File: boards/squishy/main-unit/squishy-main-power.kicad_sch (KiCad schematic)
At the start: 159 parts, among them J5 Jack-DC, Q1 NTMFS5C442NT1G, Q10 PFET, Q2 NX6008NBKR, Q3 NX6008NBKR, Q4 NX6008NBKR, Q5 NX6008NBKR, Q6 PMPB20EN, Q8 DMN65D8L-7, SW1 RST, U1 LFE5UM5G-45F-8BG381C, U13 LM51551DSSR, U18 HyperRAM, U19 HyperRAM, U2 GD25Q64EWIGR, U21 AP3428/A, U5 APX811-40UG-7, U7 TPS73733DRVR, U8 TPS7A1125PDRVT, U9 TPS7A1112PDRVT

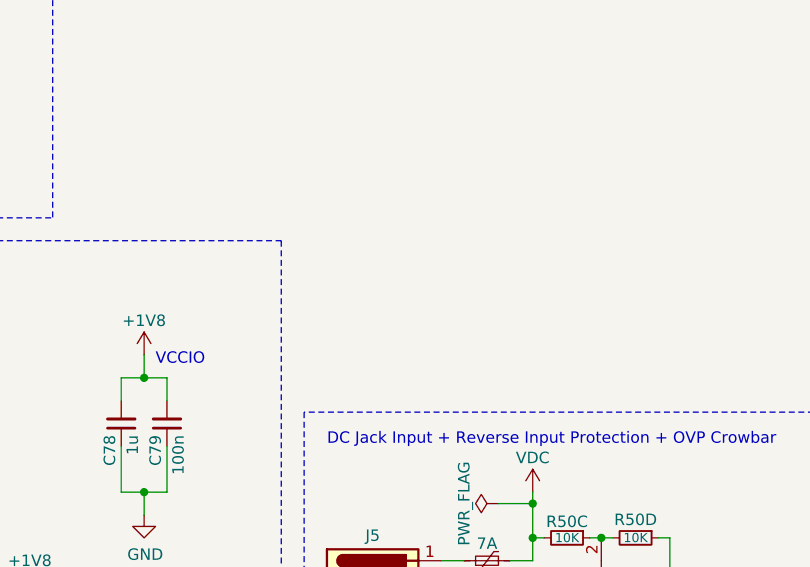
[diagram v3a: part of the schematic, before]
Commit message: squishy: main: Cleaned up the SCSI PHY current sense stuff and de-brain-sluged the PHY connector
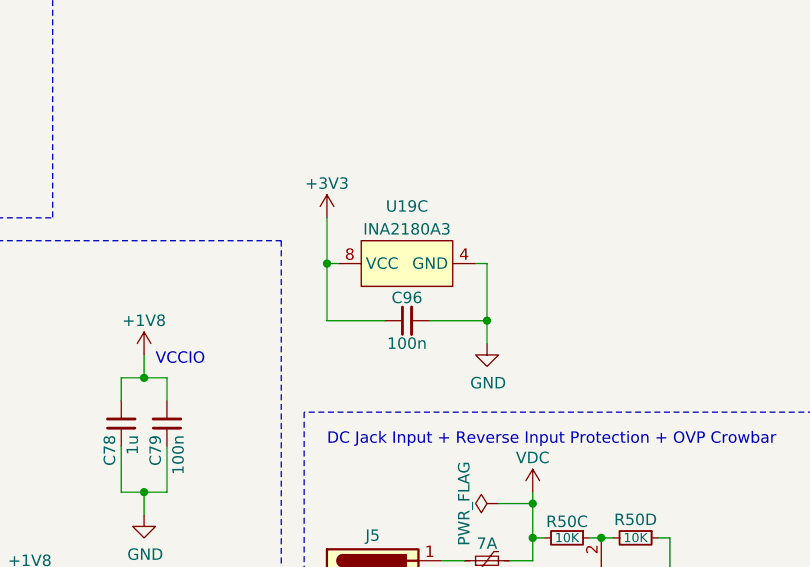
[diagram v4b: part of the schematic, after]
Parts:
- added C96: 100n, Capacitor_SMD:C_0603_1608Metric, symbol Device:C_Small
- added unit 3 of U19
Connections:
- net +3V3: now also C96.1, U19.8 (VCC)
- net GND: now also C96.2, U19.4 (GND), U19.9 (GND)
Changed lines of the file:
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@@
   (junction (at 69.85 259.08) (diameter 0) (color 0 0 0 0)
   )
+  (junction (at 173.99 96.52) (diameter 0) (color 0 0 0 0)
+  )
   (junction (at 207.01 208.28) (diameter 0) (color 0 0 0 0)
   )
@@
   (junction (at 57.15 138.43) (diameter 0) (color 0 0 0 0)
   )
+  (junction (at 156.21 90.17) (diameter 0) (color 0 0 0 0)
+  )
   (junction (at 116.84 137.16) (diameter 0) (color 0 0 0 0)
   )
@@
     (stroke (width 0) (type default))
   )
+  (wire (pts (xy 156.21 85.09) (xy 156.21 90.17))
+    (stroke (width 0) (type default))
+  )
   (polyline (pts (xy 201.93 146.05) (xy 201.93 182.88))
     (stroke (width 0) (type dash))
@@
     (stroke (width 0) (type default))
   )
+  (wire (pts (xy 167.64 96.52) (xy 173.99 96.52))
+    (stroke (width 0) (type default))
+  )
   (polyline (pts (xy 377.19 146.05) (xy 377.19 132.08))
     (stroke (width 0) (type dash))
@@
     (stroke (width 0) (type default))
   )
+  (wire (pts (xy 156.21 90.17) (xy 156.21 96.52))
+    (stroke (width 0) (type default))
+  )
   (wire (pts (xy 233.68 163.83) (xy 233.68 166.37))
     (stroke (width 0) (type default))
@@
     (stroke (width 0) (type default))
   )
+  (wire (pts (xy 156.21 90.17) (xy 157.48 90.17))
+    (stroke (width 0) (type default))
+  )
   (wire (pts (xy 76.2 36.83) (xy 76.2 39.37))
     (stroke (width 0) (type default))
@@
     (stroke (width 0) (type default))
   )
+  (wire (pts (xy 173.99 96.52) (xy 173.99 99.06))
+    (stroke (width 0) (type default))
+  )
   (wire (pts (xy 281.94 182.88) (xy 289.56 182.88))
     (stroke (width 0) (type default))
@@
     (stroke (width 0) (type default))
   )
+  (wire (pts (xy 173.99 90.17) (xy 173.99 96.52))
+    (stroke (width 0) (type default))
+  )
   (wire (pts (xy 391.16 137.16) (xy 393.7 137.16))
     (stroke (width 0) (type default))
@@
     (stroke (width 0) (type default))
   )
+  (wire (pts (xy 156.21 96.52) (xy 162.56 96.52))
+    (stroke (width 0) (type default))
+  )
   (wire (pts (xy 208.28 267.97) (xy 208.28 271.78))
     (stroke (width 0) (type default))
@@
     (stroke (width 0) (type default))
   )
+  (wire (pts (xy 172.72 90.17) (xy 173.99 90.17))
+    (stroke (width 0) (type default))
+  )
   (wire (pts (xy 55.88 186.69) (xy 63.5 186.69))
     (stroke (width 0) (type default))
@@
     )
   )
+  (symbol (lib_id "power:GND") (at 173.99 99.06 0) (unit 1)
+    (in_bom yes) (on_board yes) (dnp no)
+    (property "Reference" "#PWR0147" (at 173.99 105.41 0)
+      (effects (font (size 1.27 1.27)) hide)
+    )
+    (property "Value" "GND" (at 174.117 103.4542 0)
+      (effects (font (size 1.27 1.27)))
+    )
+    (property "Footprint" "" (at 173.99 99.06 0)
+      (effects (font (size 1.27 1.27)) hide)
+    )
+    (property "Datasheet" "" (at 173.99 99.06 0)
+      (effects (font (size 1.27 1.27)) hide)
+    )
+    (pin "1")
+    (instances
+      (project "squishy-main"
+        (path "/d4567381-92dd-4d3b-8c64-40007ced30aa/3a0401a0-2db0-4f5c-bc8b-66f50b74dd32"
+          (reference "#PWR0147") (unit 1)
+        )
+      )
+    )
+  )
   (symbol (lib_id "DX-MON:pkl_R4_Small") (at 20.32 43.18 180) (unit 4)
     (in_bom yes) (on_board yes) (dnp no)
@@
     )
   )
+  (symbol (lib_id "Device:C_Small") (at 165.1 96.52 90) (unit 1)
+    (in_bom yes) (on_board yes) (dnp no)
+    (property "Reference" "C96" (at 165.1 93.98 90)
+      (effects (font (size 1.27 1.27)))
+    )
+    (property "Value" "100n" (at 165.1 99.06 90)
+      (effects (font (size 1.27 1.27)))
+    )
+    (property "Footprint" "Capacitor_SMD:C_0603_1608Metric" (at 165.1 96.52 0)
+      (effects (font (size 1.27 1.27)) hide)
+    )
+    (property "Datasheet" "https://content.kemet.com/datasheets/KEM_C1006_X5R_SMD.pdf" (at 165.1 96.52 0)
+      (effects (font (size 1.27 1.27)) hide)
+    )
+    (property "MFR" "KEMET" (at 165.1 96.52 90)
+      (effects (font (size 1.27 1.27)) hide)
+    )
+    (property "MPN" "C0402C104M8PACTU" (at 165.1 96.52 90)
+      (effects (font (size 1.27 1.27)) hide)
+    )
+    (pin "1")
+    (pin "2")
+    (instances
+      (project "squishy-main"
+        (path "/d4567381-92dd-4d3b-8c64-40007ced30aa/3a0401a0-2db0-4f5c-bc8b-66f50b74dd32"
+          (reference "C96") (unit 1)
+        )
+      )
+    )
+  )
   (symbol (lib_id "Mechanical:MountingHole_Pad") (at 391.16 132.08 0) (unit 1)
     (in_bom no) (on_board yes) (dnp no)
@@
     )
   )
+  (symbol (lib_name "INAx180_1") (lib_id "lethalbit-analog:INAx180") (at 165.1 90.17 0) (unit 3)
+    (in_bom yes) (on_board yes) (dnp no)
+    (property "Reference" "U19" (at 165.1 83.82 0)
+      (effects (font (size 1.27 1.27)))
+    )
+    (property "Value" "INA2180A3" (at 165.1 86.36 0)
+      (effects (font (size 1.27 1.27)))
+    )
+    (property "Footprint" "lethalbit:WSON_8_2x2mm_1EP" (at 165.1 81.28 0)
+      (effects (font (size 1.27 1.27)) hide)
+    )
+    (property "Datasheet" "https://www.ti.com/lit/ds/symlink/ina2180.pdf" (at 165.1 81.28 0)
+      (effects (font (size 1.27 1.27)) hide)
+    )
+    (property "MFR" "Texas Instruments" (at 165.1 81.28 0)
+      (effects (font (size 1.27 1.27)) hide)
+    )
+    (property "MPN" "INA2180A3IDSGR" (at 165.1 81.28 0)
+      (effects (font (size 1.27 1.27)) hide)
+    )
+    (pin "1")
+    (pin "2")
+    (pin "3")
+    (pin "5")
+    (pin "6")
+    (pin "7")
+    (pin "4")
+    (pin "8")
+    (pin "9")
+    (instances
+      (project "squishy-main"
+        (path "/d4567381-92dd-4d3b-8c64-40007ced30aa/3a0401a0-2db0-4f5c-bc8b-66f50b74dd32"
+          (reference "U19") (unit 3)
+        )
+      )
+    )
+  )
   (symbol (lib_id "power:GND") (at 223.52 175.26 0) (unit 1)
     (in_bom yes) (on_board yes) (dnp no)
@@
         )
       )
+    )
+  )
+  (symbol (lib_id "power:+3V3") (at 156.21 85.09 0) (unit 1)
+    (in_bom yes) (on_board yes) (dnp no)
+    (property "Reference" "#PWR0148" (at 156.21 88.9 0)
+      (effects (font (size 1.27 1.27)) hide)
+    )
+    (property "Value" "+3V3" (at 156.21 81.28 0)
+      (effects (font (size 1.27 1.27)))
+    )
+    (property "Footprint" "" (at 156.21 85.09 0)
+      (effects (font (size 1.27 1.27)) hide)
+    )
+    (property "Datasheet" "" (at 156.21 85.09 0)
+      (effects (font (size 1.27 1.27)) hide)
+    )
+    (pin "1")
+    (instances
+      (project "squishy-main"
+        (path "/d4567381-92dd-4d3b-8c64-40007ced30aa/3a0401a0-2db0-4f5c-bc8b-66f50b74dd32"
+          (reference "#PWR0148") (unit 1)
+        )
+      )

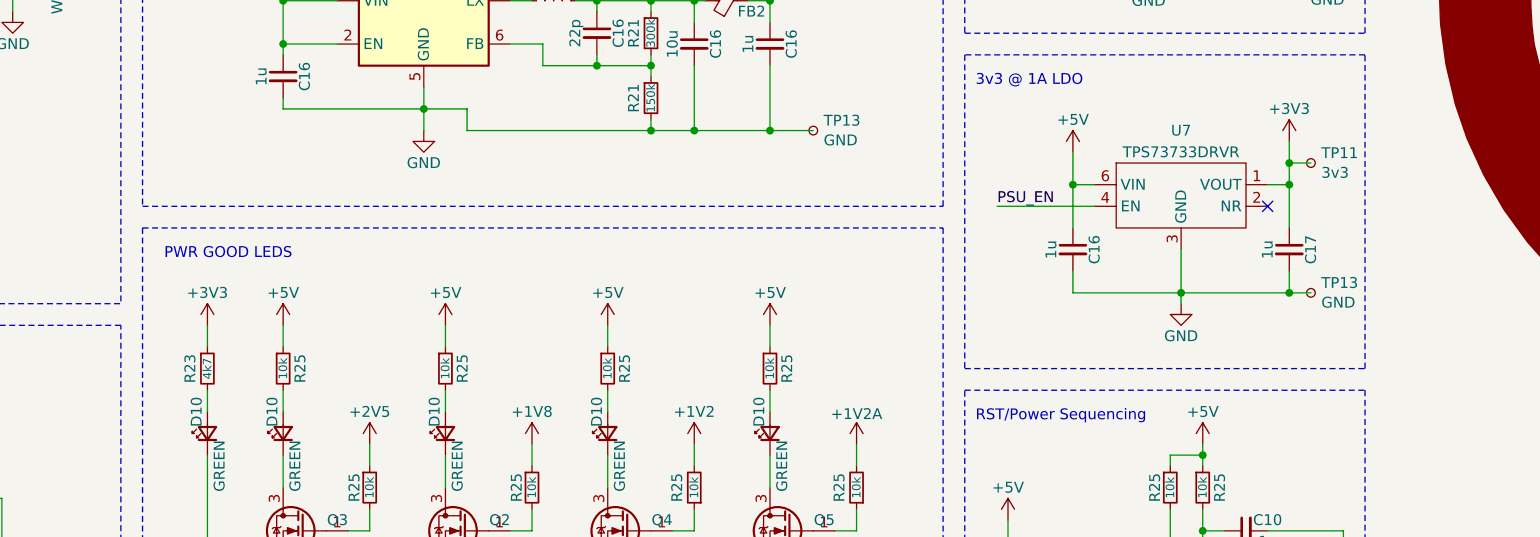
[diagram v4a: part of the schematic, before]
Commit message: squishy: main: Added notes about if we really want the 1v8 buck hanging off the 3v3 LDO, and that we might need to up the 3v3 LDO from 1A to larger
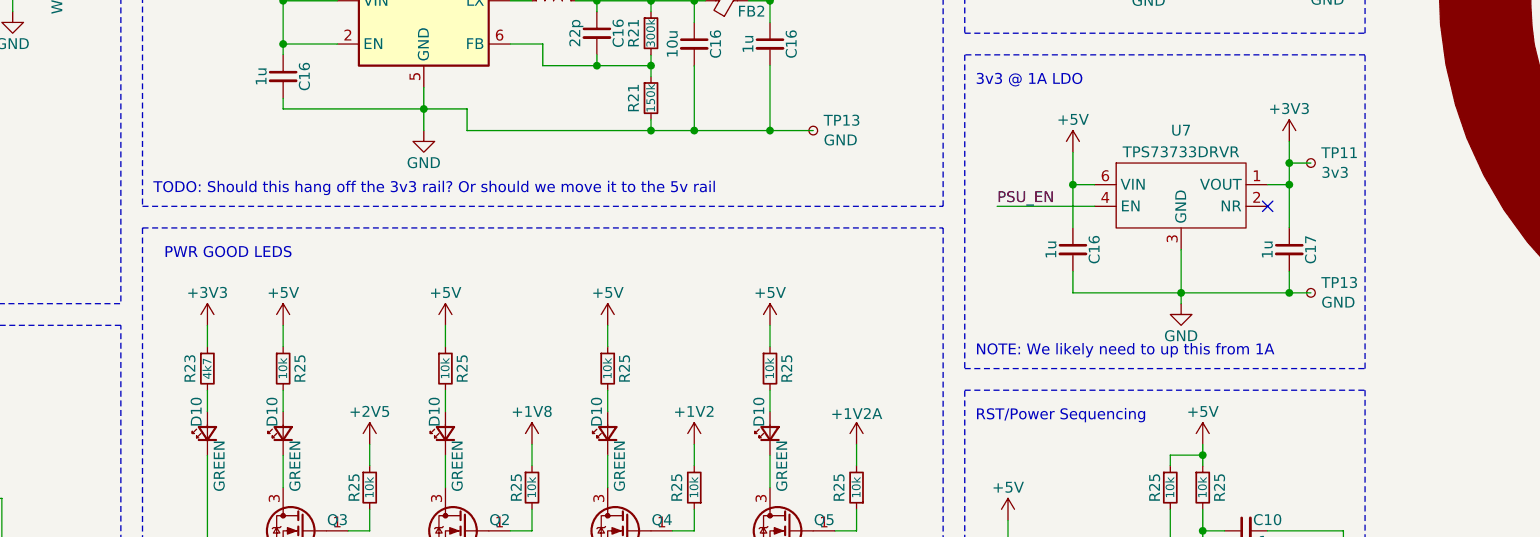
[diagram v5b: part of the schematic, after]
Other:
- note added: "NOTE: We likely need to up this from 1A"
- note added: "TODO: Should this hang off the 3v3 rail? Or should we move it to the 5v rail"
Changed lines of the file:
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@@
+    (effects (font (size 1.27 1.27)) (justify left bottom))
+  )
+  (text "NOTE: We likely need to up this from 1A\n" (at 251.46 242.57 0)
     (effects (font (size 1.27 1.27)) (justify left bottom))
   )
@@
     (effects (font (size 1.27 1.27)) (justify left bottom))
   )
+  (text "TODO: Should this hang off the 3v3 rail? Or should we move it to the 5v rail"
+    (at 154.94 223.52 0)
+    (effects (font (size 1.27 1.27)) (justify left bottom))
+  )

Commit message: squishy: main: Some final cleanup, made ERC clean, hooked up some more rough ordering for IO pins for the SCSI PHY, Replaced the 3v3 LDO with a buck due to other rails hanging off of it.
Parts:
- removed C16, C17: 1u, Capacitor_SMD:C_0603_1608Metric, symbol Device:C_Small
- removed TP13: GND, TestPoint:TestPoint_Pad_D1.0mm, symbol Connector:TestPoint_Small
- removed U7: TPS73733DRVR, Package_SON:WSON-6-1EP_2x2mm_P0.65mm_EP1x1.6mm, symbol lethalbit-power:TPS737xx
- added C101: 22u, Capacitor_SMD:C_0603_1608Metric, symbol Device:C_Small
- added C46: 10u, Capacitor_SMD:C_0603_1608Metric, symbol Device:C_Small
- added L3: 1u, lethalbit-inductor:L_Vishay_IHLP-3232, symbol Device:L
- added R55: 249k, Resistor_SMD:R_0603_1608Metric, symbol Device:R_Small
- added R56: 39k2, Resistor_SMD:R_0603_1608Metric, symbol Device:R_Small
- added R57: 178k, Resistor_SMD:R_0603_1608Metric, symbol Device:R_Small
- added TP47: SEPIC_GOOD, TestPoint:TestPoint_Pad_D1.0mm, symbol Connector:TestPoint_Small
- added TP7: GND, TestPoint:TestPoint_Pad_D1.0mm, symbol Connector:TestPoint_Small
- added U23: TLV62084ADSGx, Package_SON:WSON-8-1EP_2x2mm_P0.5mm_EP0.9x1.6mm, symbol Regulator_Switching:TLV62084ADSGx
- U19: value INA2180A3 -> INA2180A1; MPN INA2180A3IDSGR -> INA2180A1IDSGR
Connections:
- net +1V2: no longer C33.1, R25.2, TP12.1, U1.T15 (VCCA1), U1.T6 (VCCA0), U1.U15 (VCCA1), U1.U6 (VCCA0), U8.3 (EN), U9.1 (VOUT), U9.2 (NC)
- net +3V3: now also U1.F10 (VCCIO0), U1.F11 (VCCIO1), U1.F12 (VCCIO1), U1.F9 (VCCIO0), U1.H6 (VCCIO7), U1.H7 (VCCIO7), U1.J6 (VCCIO7), C101.1, L3.2, R55.2, R57.1, U23.5 (VOS); no longer C16.1, U21.3 (VIN)
- net +5V: now also C16.1, U21.3 (VIN), C46.1, U23.8 (VIN)
- net GND: now also C101.2, C46.2, R56.2, TP7.1, U23.2 (GND), U23.3 (GND), U23.9 (GND)
- net PSU_EN: now also U23.1 (EN)
- net SEPIC_GOOD: now also TP47.1
- new net: L3.1, U23.7 (SW)
- new net: R57.2, U23.6 (PG)
- new net: R55.1, R56.1, U23.4 (FB)
- new net +1V2A: C33.1, R25.2, TP12.1, U1.T15 (VCCA1), U1.T6 (VCCA0), U1.U15 (VCCA1), U1.U6 (VCCA0), U8.3 (EN), U9.1 (VOUT), U9.2 (NC)
- no-connect marks 3 -> 2
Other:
- note added: "3v3 Buck"
- note added: "CSA"
- note removed: "3v3 @ 1A LDO"
- note removed: "NOTE: We likely need to up this from 1A"
- note removed: "TODO: Should this hang off the 3v3 rail? Or should we move it to the 5v rail"
- moved on the sheet: C16, C27, C32, C33, C96, FB2, L2, R21, TP11, TP12, TP13, TP17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

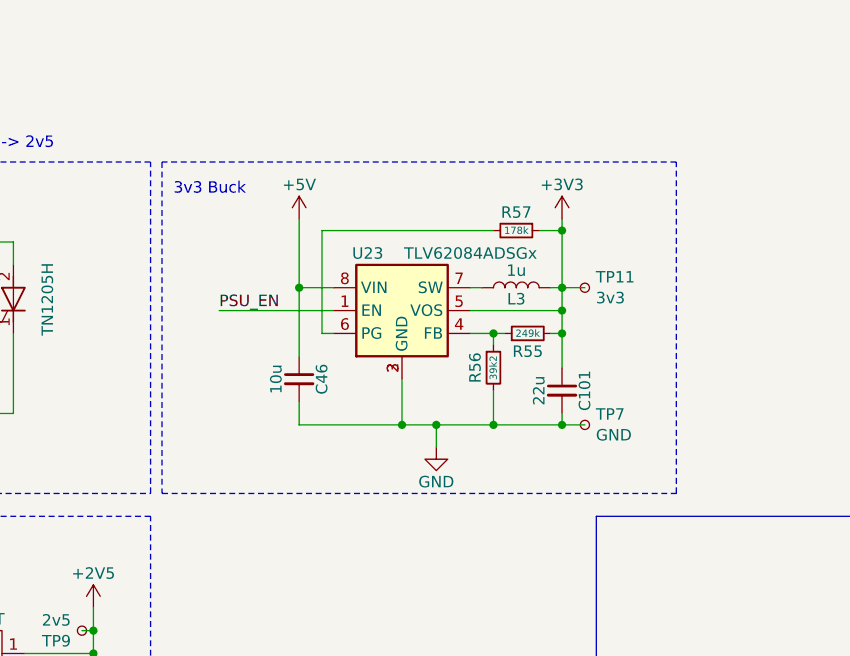
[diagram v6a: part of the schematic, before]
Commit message: squishy: main: Added the missing footprint for Q7
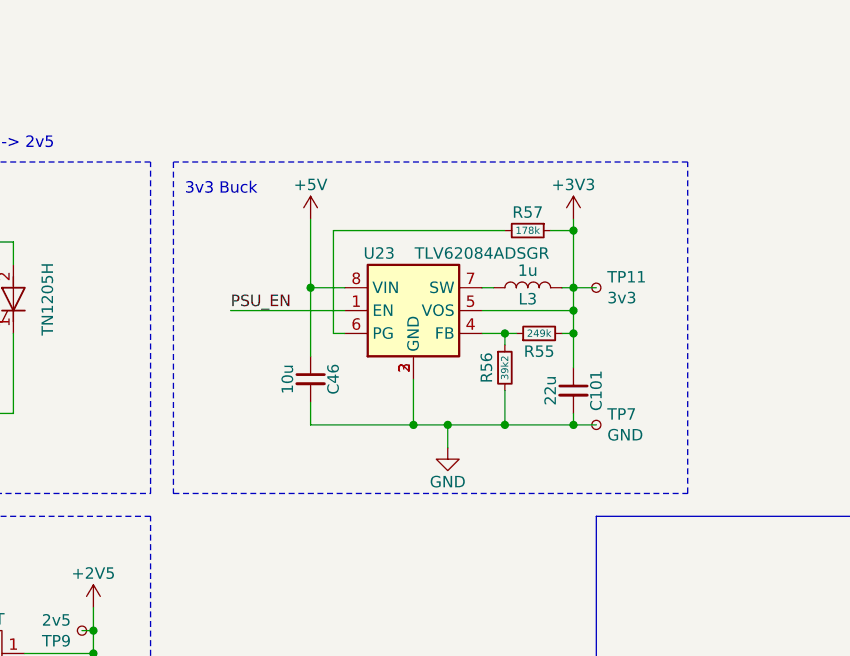
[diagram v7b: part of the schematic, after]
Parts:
- U23: value TLV62084ADSGx -> TLV62084ADSGR
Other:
- moved on the sheet: C101, C46, L3, R55, R56, R57, TP11, TP7, U23
